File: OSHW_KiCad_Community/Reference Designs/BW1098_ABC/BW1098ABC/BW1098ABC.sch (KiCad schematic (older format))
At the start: 10 parts

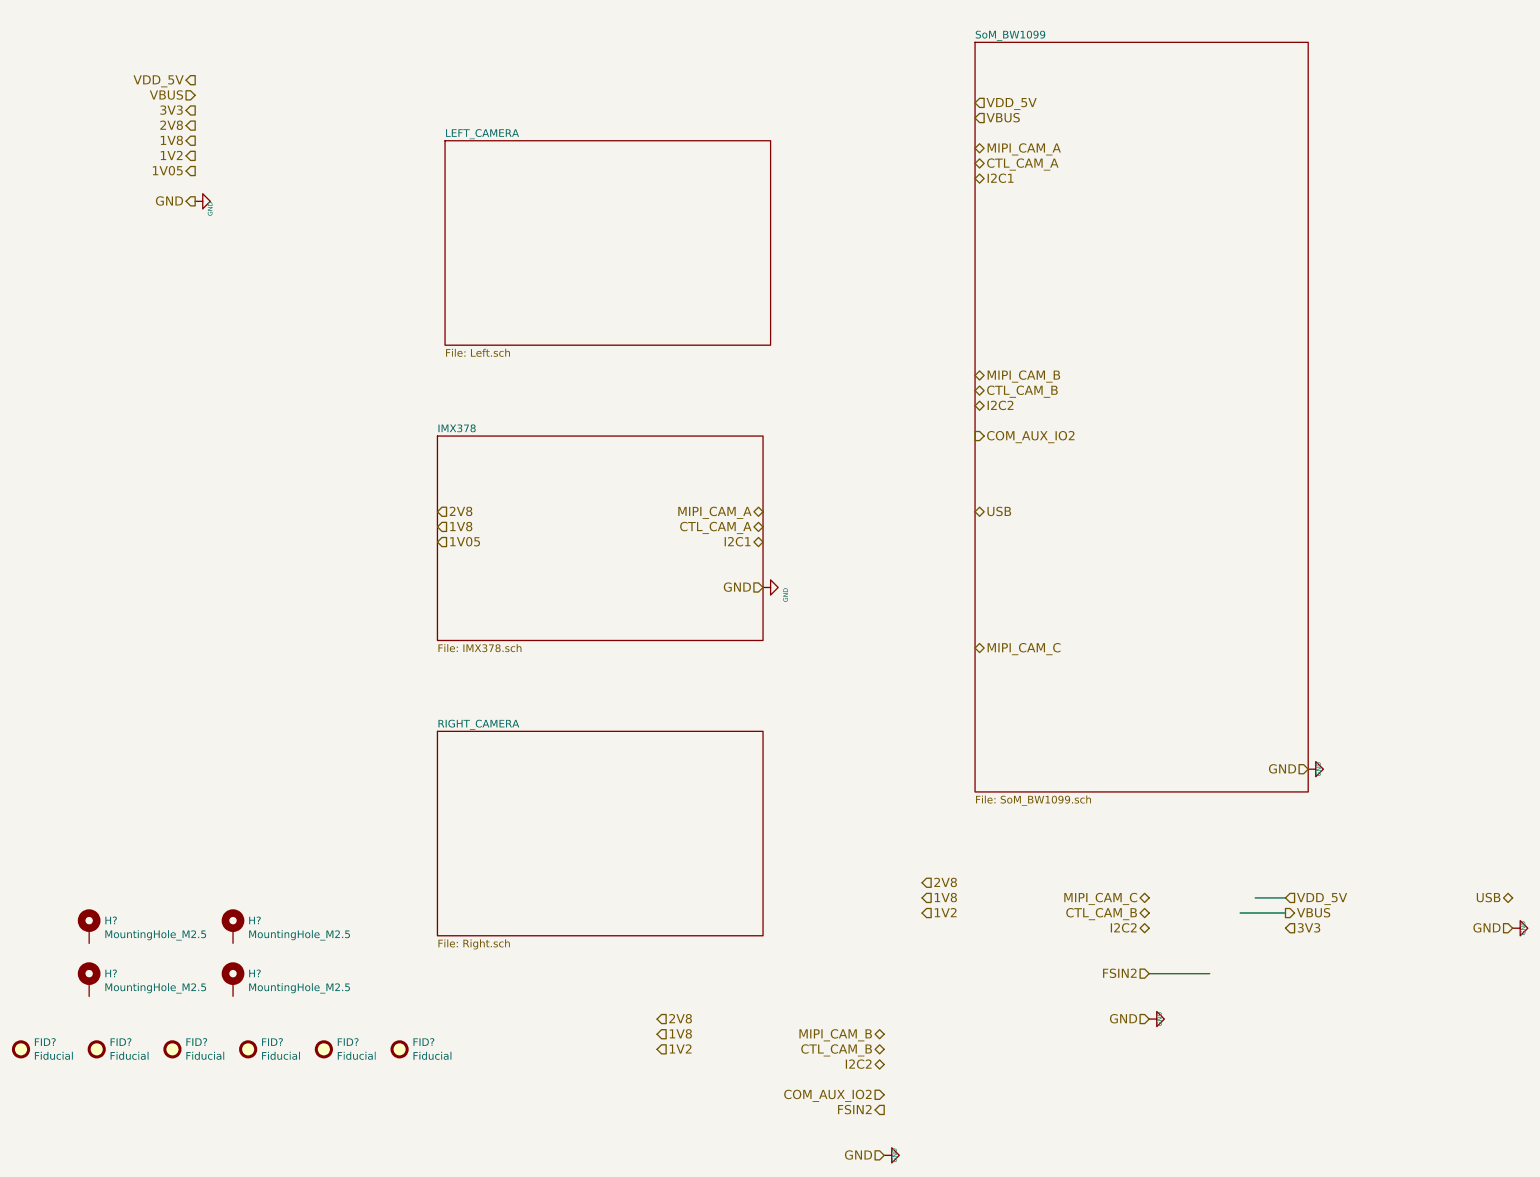
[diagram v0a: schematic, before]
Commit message: skeleton complete, most footprints assigned, still need to check the transferred ones for dims
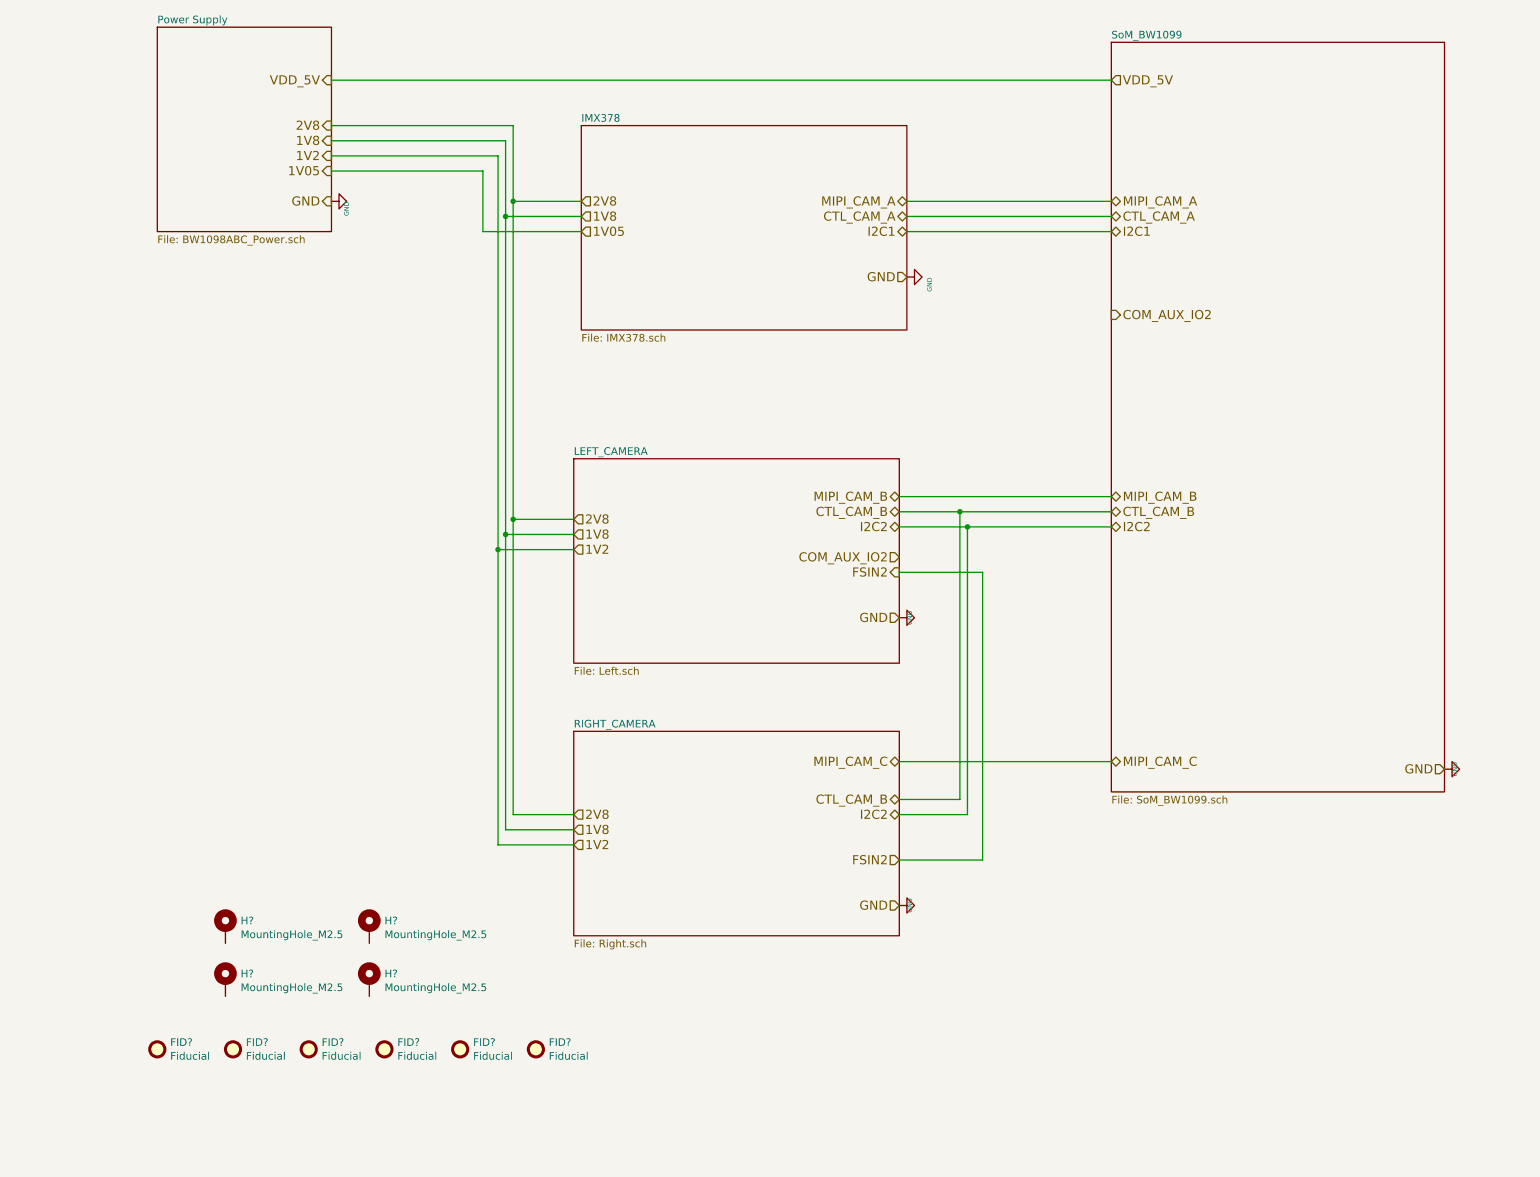
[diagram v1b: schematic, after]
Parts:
- removed FID? (x4): Fiducial, symbol Mechanical:Fiducial
- added FID? (x4): Fiducial, Fiducial:Fiducial_1mm_Mask2mm, symbol Mechanical:Fiducial
- FID? (x2): footprint (none) -> Fiducial:Fiducial_1mm_Mask2mm
- H? (x4): footprint (none) -> fp_luxonis:Mounting_Wuerth_WA-SMSI-M2_H3mm_9774030243
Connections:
- net labels removed: 3V3, USB, VBUS
- wire segments 3 -> 39
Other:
- moved on the sheet: FID?, H?

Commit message: small stuff
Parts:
- H? (x4): symbol depthAI_sch:Mechanical_MountingHole_Pad -> BW1098ABC-rescue:Mechanical_MountingHole_Pad-depthAI_sch
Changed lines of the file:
@@
 $EndComp
 $Comp
-L depthAI_sch:Mechanical_MountingHole_Pad H?
+L BW1098ABC-rescue:Mechanical_MountingHole_Pad-depthAI_sch H?
 U 1 1 5FF5350B
 P 2200 6700
@@
 $EndComp
 $Comp
-L depthAI_sch:Mechanical_MountingHole_Pad H?
+L BW1098ABC-rescue:Mechanical_MountingHole_Pad-depthAI_sch H?
 U 1 1 5FF56FF7
 P 2200 7050
@@
 $EndComp
 $Comp
-L depthAI_sch:Mechanical_MountingHole_Pad H?
+L BW1098ABC-rescue:Mechanical_MountingHole_Pad-depthAI_sch H?
 U 1 1 5FF572C3
 P 3150 7050
@@
 $EndComp
 $Comp
-L depthAI_sch:Mechanical_MountingHole_Pad H?
+L BW1098ABC-rescue:Mechanical_MountingHole_Pad-depthAI_sch H?
 U 1 1 5FF57937
 P 3150 6700
